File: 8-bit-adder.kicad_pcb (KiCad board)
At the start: 2 copper layers, 109.2 x 88.9 mm, 211 parts, among them J1 J2-2_pole_connector, J2 J8-8_bit_bus_connector, J3 J8-8_bit_bus_connector, J4 J8-8_bit_bus_connector, J5 J1-1_bit_bus, Q1 2N7000, Q10 2N7000, Q100 2N7000, Q101 2N7000, Q102 2N7000, Q103 2N7000, Q104 2N7000, Q105 2N7000, Q106 2N7000, Q107 2N7000, Q108 2N7000, Q109 2N7000, Q11 2N7000, Q110 2N7000, Q111 2N7000, Q112 2N7000, Q113 2N7000, Q114 2N7000, Q115 2N7000, Q116 2N7000, Q117 2N7000, Q118 2N7000, Q119 2N7000, Q12 2N7000, Q13 2N7000, Q14 2N7000, Q15 2N7000, Q16 2N7000, Q17 2N7000, Q18 2N7000, Q19 2N7000, Q2 2N7000, Q20 2N7000, Q21 2N7000, Q22 2N7000, Q23 2N7000, Q24 2N7000, Q25 2N7000, Q26 2N7000, Q27 2N7000, Q28 2N7000, Q29 2N7000, Q3 2N7000, Q30 2N7000, Q31 2N7000, Q32 2N7000, Q33 2N7000, Q34 2N7000, Q35 2N7000, Q36 2N7000, Q37 2N7000, Q38 2N7000, Q39 2N7000, Q4 2N7000, Q40 2N7000, Q41 2N7000, Q42 2N7000, Q43 2N7000, Q44 2N7000, Q45 2N7000, Q46 2N7000, Q47 2N7000, Q48 2N7000, Q49 2N7000, Q5 2N7000, Q50 2N7000, Q51 2N7000, Q52 2N7000, Q53 2N7000, Q54 2N7000, Q55 2N7000, Q56 2N7000, Q57 2N7000, Q58 2N7000, Q59 2N7000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

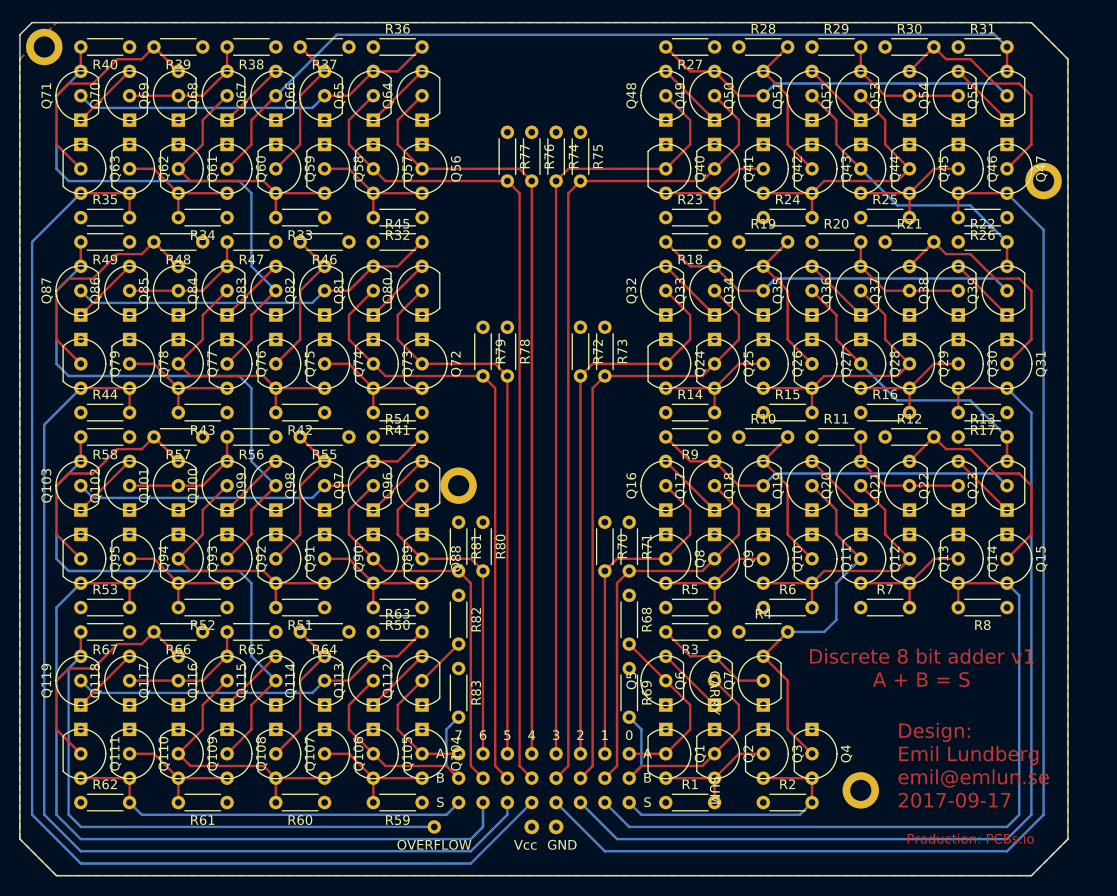
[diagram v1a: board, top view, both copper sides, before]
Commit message: Add carry input to 8 bit adder
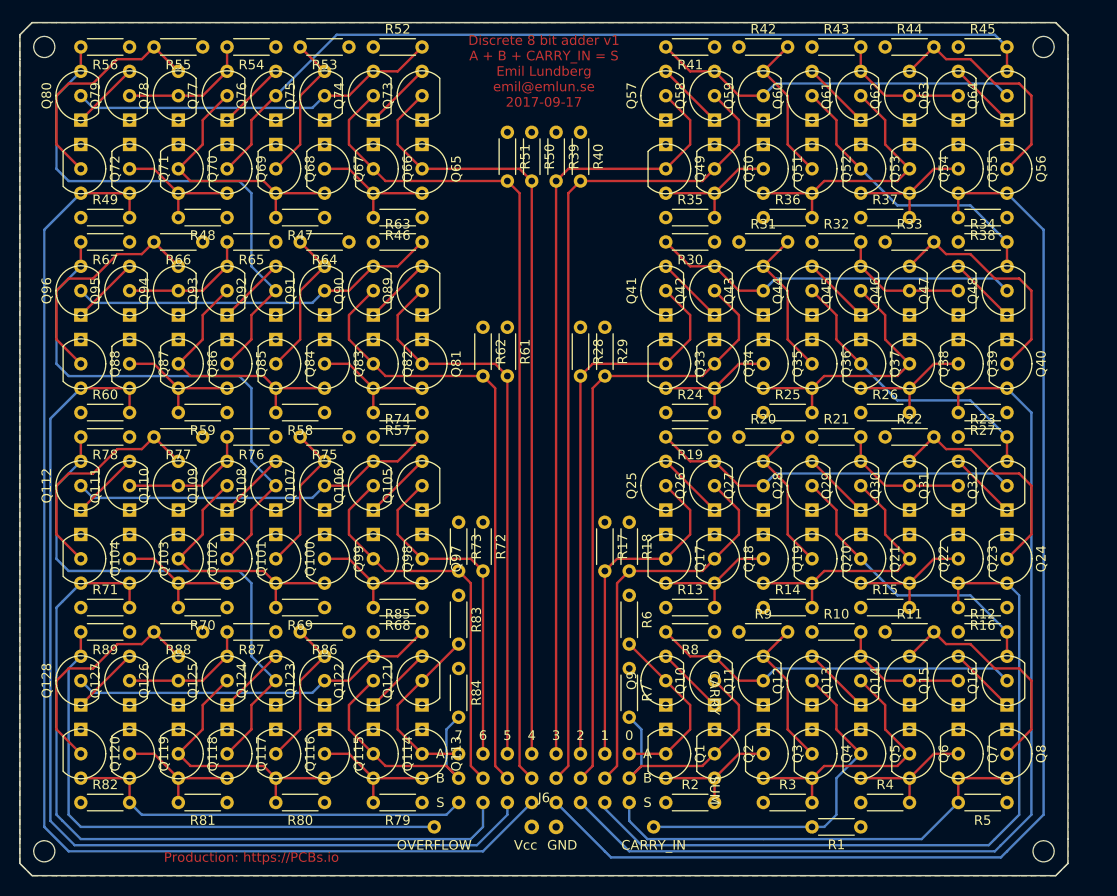
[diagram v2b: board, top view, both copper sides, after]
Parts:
- removed the REF** at (210.8, 77.5)
- removed the REF** at (106.7, 63.5)
- removed the REF** at (149.9, 109.2)
- removed the REF** at (191.8, 141.0)
- added J6: J8-8_bit_bus_connector, emlun:J8-8_bit_bus_connector, F.Cu at (158.8, 142.2)
- added Q120: 2N7000, electrokit:TO-92_Molded_Wide_Inline, F.Cu at (110.5, 135.9)
- added Q121: 2N7000, electrokit:TO-92_Molded_Wide_Inline, F.Cu at (146.1, 130.8)
- added Q122: 2N7000, electrokit:TO-92_Molded_Wide_Inline, F.Cu at (141.0, 130.8)
- added Q123: 2N7000, electrokit:TO-92_Molded_Wide_Inline, F.Cu at (135.9, 130.8)
- added Q124: 2N7000, electrokit:TO-92_Molded_Wide_Inline, F.Cu at (130.8, 130.8)
- added Q125: 2N7000, electrokit:TO-92_Molded_Wide_Inline, F.Cu at (125.7, 130.8)
- added Q126: 2N7000, electrokit:TO-92_Molded_Wide_Inline, F.Cu at (120.7, 130.8)
- added Q127: 2N7000, electrokit:TO-92_Molded_Wide_Inline, F.Cu at (115.6, 130.8)
- added Q128: 2N7000, electrokit:TO-92_Molded_Wide_Inline, F.Cu at (110.5, 130.8)
- added R84: 1M, Resistors_THT:R_Axial_DIN0204_L3.6mm_D1.6mm_P5.08mm_Horizontal, F.Cu at (149.9, 128.3)
- added R85: 1M, Resistors_THT:R_Axial_DIN0204_L3.6mm_D1.6mm_P5.08mm_Horizontal, F.Cu at (141.0, 124.5)
- added R86: 1M, Resistors_THT:R_Axial_DIN0204_L3.6mm_D1.6mm_P5.08mm_Horizontal, F.Cu at (138.4, 124.5)
- added R87: 1M, Resistors_THT:R_Axial_DIN0204_L3.6mm_D1.6mm_P5.08mm_Horizontal, F.Cu at (130.8, 124.5)
- added R88: 1M, Resistors_THT:R_Axial_DIN0204_L3.6mm_D1.6mm_P5.08mm_Horizontal, F.Cu at (123.2, 124.5)
- added R89: 1M, Resistors_THT:R_Axial_DIN0204_L3.6mm_D1.6mm_P5.08mm_Horizontal, F.Cu at (115.6, 124.5)
- added REF**: MountingHole_2.2mm_M2_ISO14580, Mounting_Holes:MountingHole_2.2mm_M2_ISO14580, F.Cu at (210.8, 147.3)
- added REF**: MountingHole_2.2mm_M2, Mounting_Holes:MountingHole_2.2mm_M2, F.Cu at (210.8, 63.5)
- added REF**: MountingHole_2.2mm_M2, Mounting_Holes:MountingHole_2.2mm_M2, F.Cu at (106.7, 63.5)
- added REF**: MountingHole_2.2mm_M2, Mounting_Holes:MountingHole_2.2mm_M2, F.Cu at (106.7, 147.3)
- J2: value J8-8_bit_bus_connector -> J1-1_bit_bus; footprint emlun:J8-8_bit_bus_connector -> emlun:J1-1_bit_bus
- moved R44 92.1 mm to (194.3, 63.5)
- moved Q63 91.6 mm to (201.9, 69.8), turned to 90 degrees
- moved Q62 81.4 mm to (196.8, 69.8), turned to 90 degrees
- moved R38 78.2 mm to (207.0, 81.3)
- moved R34 76.2 mm to (201.9, 83.8), turned to 0 degrees
- moved R43 71.9 mm to (186.7, 63.5), turned to 0 degrees
- moved Q61 71.3 mm to (191.8, 69.8), turned to 90 degrees
- moved R62 64.9 mm to (152.4, 92.7), turned to 270 degrees
- moved R53 64.8 mm to (138.4, 63.5), turned to 180 degrees
- moved R45 64.3 mm to (201.9, 63.5)
- moved Q60 61.2 mm to (186.7, 69.8), turned to 90 degrees
- moved R35 61.0 mm to (171.4, 81.3)
- moved Q56 61.0 mm to (207.0, 74.9)
- moved Q64 61.0 mm to (207.0, 69.8)
- moved R52 60.4 mm to (141.0, 63.5), turned to 0 degrees
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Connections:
- J2 pad 1: /a1 -> /c
- J3 pad 0: /S0 -> /a0
- J3 pad 1: /S1 -> /a1
- J3 pad 2: /S2 -> /a2
- J3 pad 3: /S3 -> /a3
- J3 pad 4: /S4 -> /a4
- J3 pad 5: /S5 -> /a5
- J3 pad 6: /S6 -> /a6
- J3 pad 7: /S7 -> /a7
- J4 pad 0: /b0 -> /S0
- J4 pad 1: /b1 -> /S1
- J4 pad 2: /b2 -> /S2
- J4 pad 3: /b3 -> /S3
- J4 pad 4: /b4 -> /S4
- J4 pad 5: /b5 -> /S5
- J4 pad 6: /b6 -> /S6
- J4 pad 7: /b7 -> /S7
- Q10 pad 1: GND -> Net-(Q10-Pad1)
- Q10 pad 2: Net-(Q10-Pad2) -> /b0
- Q100 pad 1: Net-(Q100-Pad1) -> GND
- Q101 pad 2: Net-(Q100-Pad3) -> /C5
- Q102 pad 3: Net-(Q102-Pad3) -> Net-(Q101-Pad3)
- Q103 pad 1: Net-(Q102-Pad3) -> GND
- Q103 pad 2: Net-(Q103-Pad2) -> Net-(Q101-Pad3)
- Q103 pad 3: /C6 -> /S6
- Q104 pad 2: /a7 -> Net-(Q104-Pad2)
- Q104 pad 3: Net-(Q104-Pad3) -> /S6
- Q105 pad 2: /b7 -> /a6
- Q105 pad 3: Net-(Q104-Pad3) -> Net-(Q105-Pad3)
- Q106 pad 1: GND -> Net-(Q105-Pad3)
- Q106 pad 2: Net-(Q104-Pad3) -> /b6
- Q107 pad 2: Net-(Q107-Pad2) -> Net-(Q106-Pad3)
- Q107 pad 3: Net-(Q106-Pad3) -> Net-(Q100-Pad2)
- Q108 pad 2: /C6 -> /C5
- Q109 pad 1: GND -> Net-(Q108-Pad3)
- Q109 pad 2: Net-(Q106-Pad3) -> Net-(Q100-Pad3)
- Q109 pad 3: Net-(Q108-Pad3) -> Net-(Q109-Pad3)
- Q11 pad 2: Net-(Q11-Pad2) -> Net-(Q10-Pad3)
- Q11 pad 3: Net-(Q10-Pad3) -> Net-(Q11-Pad3)
- Q110 pad 2: Net-(Q108-Pad3) -> Net-(Q109-Pad3)
- Q110 pad 3: /S7 -> Net-(Q104-Pad2)
- Q111 pad 2: Net-(Q111-Pad2) -> Net-(Q109-Pad3)
- Q111 pad 3: /S7 -> Net-(Q111-Pad3)
- Q112 pad 1: GND -> Net-(Q111-Pad3)
- Q112 pad 2: /a7 -> Net-(Q106-Pad3)
- Q112 pad 3: Net-(Q112-Pad3) -> /C6
- Q113 pad 1: Net-(Q112-Pad3) -> GND
- Q113 pad 2: /b7 -> /a7
- Q114 pad 2: Net-(Q113-Pad3) -> /b7
- Q114 pad 3: Net-(Q107-Pad2) -> Net-(Q113-Pad3)
- Q115 pad 2: /C6 -> Net-(Q113-Pad3)
- Q116 pad 1: Net-(Q115-Pad3) -> GND
- Q116 pad 2: Net-(Q106-Pad3) -> Net-(Q116-Pad2)
- Q116 pad 3: Net-(Q116-Pad3) -> Net-(Q115-Pad3)
- Q117 pad 2: Net-(Q116-Pad3) -> /C6
- Q117 pad 3: Net-(Q111-Pad2) -> Net-(Q117-Pad3)
- Q118 pad 2: Net-(Q116-Pad3) -> Net-(Q115-Pad3)
- Q118 pad 3: Net-(Q118-Pad3) -> Net-(Q117-Pad3)
- Q119 pad 1: Net-(Q118-Pad3) -> GND
- Q119 pad 2: Net-(Q113-Pad3) -> Net-(Q117-Pad3)
- Q119 pad 3: /C7 -> /S7
- Q12 pad 2: /C0 -> /c
- Q13 pad 1: GND -> Net-(Q12-Pad3)
- Q13 pad 2: Net-(Q10-Pad3) -> Net-(Q13-Pad2)
- Q13 pad 3: Net-(Q12-Pad3) -> Net-(Q13-Pad3)
- Q14 pad 2: Net-(Q12-Pad3) -> Net-(Q13-Pad3)
- Q14 pad 3: /S1 -> Net-(Q14-Pad3)
- Q15 pad 2: Net-(Q15-Pad2) -> Net-(Q13-Pad3)
- Q15 pad 3: /S1 -> Net-(Q15-Pad3)
- Q16 pad 1: GND -> Net-(Q15-Pad3)
- Q16 pad 2: /a1 -> Net-(Q10-Pad3)
- Q16 pad 3: Net-(Q16-Pad3) -> /C0
- Q17 pad 1: Net-(Q16-Pad3) -> GND
- Q17 pad 2: /b1 -> /a1
- Q18 pad 2: Net-(Q17-Pad3) -> /b1
- Q18 pad 3: Net-(Q11-Pad2) -> Net-(Q17-Pad3)
- Q19 pad 2: /C0 -> Net-(Q17-Pad3)
- Q20 pad 1: Net-(Q19-Pad3) -> GND
- Q20 pad 2: Net-(Q10-Pad3) -> Net-(Q20-Pad2)
- Q20 pad 3: Net-(Q20-Pad3) -> Net-(Q19-Pad3)
- Q21 pad 2: Net-(Q20-Pad3) -> /C0
- Q21 pad 3: Net-(Q15-Pad2) -> Net-(Q21-Pad3)
- Q22 pad 2: Net-(Q20-Pad3) -> Net-(Q19-Pad3)
- Q22 pad 3: Net-(Q22-Pad3) -> Net-(Q21-Pad3)
- Q23 pad 1: Net-(Q22-Pad3) -> GND
- Q23 pad 2: Net-(Q17-Pad3) -> Net-(Q21-Pad3)
- Q23 pad 3: /C1 -> /S1
- Q24 pad 2: /a2 -> Net-(Q24-Pad2)
- Q24 pad 3: Net-(Q24-Pad3) -> /S1
- Q25 pad 2: /b2 -> /a1
- Q25 pad 3: Net-(Q24-Pad3) -> Net-(Q25-Pad3)
- Q26 pad 1: GND -> Net-(Q25-Pad3)
- Q26 pad 2: Net-(Q24-Pad3) -> /b1
- Q27 pad 2: Net-(Q27-Pad2) -> Net-(Q26-Pad3)
- Q27 pad 3: Net-(Q26-Pad3) -> Net-(Q20-Pad2)
- Q28 pad 2: /C1 -> /C0
- Q29 pad 1: GND -> Net-(Q28-Pad3)
- Q29 pad 2: Net-(Q26-Pad3) -> Net-(Q19-Pad3)
- Q29 pad 3: Net-(Q28-Pad3) -> Net-(Q29-Pad3)
- Q3 pad 3: /S0 -> Net-(Q13-Pad2)
- Q30 pad 2: Net-(Q28-Pad3) -> Net-(Q29-Pad3)
- Q30 pad 3: /S2 -> Net-(Q24-Pad2)
- Q31 pad 2: Net-(Q31-Pad2) -> Net-(Q29-Pad3)
- Q31 pad 3: /S2 -> Net-(Q31-Pad3)
- Q32 pad 1: GND -> Net-(Q31-Pad3)
- Q32 pad 2: /a2 -> Net-(Q26-Pad3)
- Q32 pad 3: Net-(Q32-Pad3) -> /C1
- Q33 pad 1: Net-(Q32-Pad3) -> GND
- Q33 pad 2: /b2 -> /a2
- Q34 pad 2: Net-(Q33-Pad3) -> /b2
- Q34 pad 3: Net-(Q27-Pad2) -> Net-(Q33-Pad3)
- Q35 pad 2: /C1 -> Net-(Q33-Pad3)
- Q36 pad 1: Net-(Q35-Pad3) -> GND
- Q36 pad 2: Net-(Q26-Pad3) -> Net-(Q36-Pad2)
- Q36 pad 3: Net-(Q36-Pad3) -> Net-(Q35-Pad3)
- Q37 pad 2: Net-(Q36-Pad3) -> /C1
- Q37 pad 3: Net-(Q31-Pad2) -> Net-(Q37-Pad3)
- Q38 pad 2: Net-(Q36-Pad3) -> Net-(Q35-Pad3)
- Q38 pad 3: Net-(Q38-Pad3) -> Net-(Q37-Pad3)
- Q39 pad 1: Net-(Q38-Pad3) -> GND
- Q39 pad 2: Net-(Q33-Pad3) -> Net-(Q37-Pad3)
- Q39 pad 3: /C2 -> /S2
- Q4 pad 2: /C0 -> Net-(Q11-Pad3)
- Q4 pad 3: /S0 -> Net-(Q13-Pad2)
- Q40 pad 2: /a3 -> Net-(Q40-Pad2)
- Q40 pad 3: Net-(Q40-Pad3) -> /S2
- Q41 pad 2: /b3 -> /a2
- Q41 pad 3: Net-(Q40-Pad3) -> Net-(Q41-Pad3)
- Q42 pad 1: GND -> Net-(Q41-Pad3)
- Q42 pad 2: Net-(Q40-Pad3) -> /b2
- Q43 pad 2: Net-(Q43-Pad2) -> Net-(Q42-Pad3)
- Q43 pad 3: Net-(Q42-Pad3) -> Net-(Q36-Pad2)
- Q44 pad 2: /C2 -> /C1
- Q45 pad 1: GND -> Net-(Q44-Pad3)
- Q45 pad 2: Net-(Q42-Pad3) -> Net-(Q35-Pad3)
- Q45 pad 3: Net-(Q44-Pad3) -> Net-(Q45-Pad3)
- Q46 pad 2: Net-(Q44-Pad3) -> Net-(Q45-Pad3)
- Q46 pad 3: /S3 -> Net-(Q40-Pad2)
- Q47 pad 2: Net-(Q47-Pad2) -> Net-(Q45-Pad3)
- Q47 pad 3: /S3 -> Net-(Q47-Pad3)
- Q48 pad 1: GND -> Net-(Q47-Pad3)
- Q48 pad 2: /a3 -> Net-(Q42-Pad3)
- Q48 pad 3: Net-(Q48-Pad3) -> /C2
- Q49 pad 1: Net-(Q48-Pad3) -> GND
- Q49 pad 2: /b3 -> /a3
- Q5 pad 2: /a0 -> /c
- Q50 pad 2: Net-(Q49-Pad3) -> /b3
- Q50 pad 3: Net-(Q43-Pad2) -> Net-(Q49-Pad3)
- Q51 pad 2: /C2 -> Net-(Q49-Pad3)
- Q52 pad 1: Net-(Q51-Pad3) -> GND
- Q52 pad 2: Net-(Q42-Pad3) -> Net-(Q52-Pad2)
- Q52 pad 3: Net-(Q52-Pad3) -> Net-(Q51-Pad3)
- Q53 pad 2: Net-(Q52-Pad3) -> /C2
- Q53 pad 3: Net-(Q47-Pad2) -> Net-(Q53-Pad3)
- Q54 pad 2: Net-(Q52-Pad3) -> Net-(Q51-Pad3)
- Q54 pad 3: Net-(Q54-Pad3) -> Net-(Q53-Pad3)
- Q55 pad 1: Net-(Q54-Pad3) -> GND
- Q55 pad 2: Net-(Q49-Pad3) -> Net-(Q53-Pad3)
- Q55 pad 3: /C3 -> /S3
- Q56 pad 2: /a4 -> Net-(Q56-Pad2)
- Q56 pad 3: Net-(Q56-Pad3) -> /S3
- Q57 pad 2: /b4 -> /a3
- Q57 pad 3: Net-(Q56-Pad3) -> Net-(Q57-Pad3)
- Q58 pad 1: GND -> Net-(Q57-Pad3)
- Q58 pad 2: Net-(Q56-Pad3) -> /b3
- Q59 pad 2: Net-(Q59-Pad2) -> Net-(Q58-Pad3)
- Q59 pad 3: Net-(Q58-Pad3) -> Net-(Q52-Pad2)
- Q6 pad 1: Net-(Q5-Pad3) -> GND
- Q6 pad 2: /b0 -> Net-(Q13-Pad2)
- Q6 pad 3: Net-(Q6-Pad3) -> Net-(Q5-Pad3)
- Q60 pad 2: /C3 -> /C2
- Q61 pad 1: GND -> Net-(Q60-Pad3)
- Q61 pad 2: Net-(Q58-Pad3) -> Net-(Q51-Pad3)
- Q61 pad 3: Net-(Q60-Pad3) -> Net-(Q61-Pad3)
- Q62 pad 2: Net-(Q60-Pad3) -> Net-(Q61-Pad3)
- Q62 pad 3: /S4 -> Net-(Q56-Pad2)
- Q63 pad 2: Net-(Q63-Pad2) -> Net-(Q61-Pad3)
- Q63 pad 3: /S4 -> Net-(Q63-Pad3)
- Q64 pad 1: GND -> Net-(Q63-Pad3)
- Q64 pad 2: /a4 -> Net-(Q58-Pad3)
- Q64 pad 3: Net-(Q64-Pad3) -> /C3
- Q65 pad 1: Net-(Q64-Pad3) -> GND
- Q65 pad 2: /b4 -> /a4
- Q66 pad 2: Net-(Q65-Pad3) -> /b4
- Q66 pad 3: Net-(Q59-Pad2) -> Net-(Q65-Pad3)
- Q67 pad 2: /C3 -> Net-(Q65-Pad3)
- Q68 pad 1: Net-(Q67-Pad3) -> GND
- Q68 pad 2: Net-(Q58-Pad3) -> Net-(Q68-Pad2)
- Q68 pad 3: Net-(Q68-Pad3) -> Net-(Q67-Pad3)
- Q69 pad 2: Net-(Q68-Pad3) -> /C3
- Q69 pad 3: Net-(Q63-Pad2) -> Net-(Q69-Pad3)
- Q7 pad 2: Net-(Q6-Pad3) -> Net-(Q5-Pad3)
- Q7 pad 3: /C0 -> /S0
- Q70 pad 2: Net-(Q68-Pad3) -> Net-(Q67-Pad3)
- Q70 pad 3: Net-(Q70-Pad3) -> Net-(Q69-Pad3)
- Q71 pad 1: Net-(Q70-Pad3) -> GND
- Q71 pad 2: Net-(Q65-Pad3) -> Net-(Q69-Pad3)
- Q71 pad 3: /C4 -> /S4
- Q72 pad 2: /a5 -> Net-(Q72-Pad2)
- Q72 pad 3: Net-(Q72-Pad3) -> /S4
- Q73 pad 2: /b5 -> /a4
- Q73 pad 3: Net-(Q72-Pad3) -> Net-(Q73-Pad3)
- Q74 pad 1: GND -> Net-(Q73-Pad3)
- Q74 pad 2: Net-(Q72-Pad3) -> /b4
- Q75 pad 2: Net-(Q75-Pad2) -> Net-(Q74-Pad3)
- Q75 pad 3: Net-(Q74-Pad3) -> Net-(Q68-Pad2)
- Q76 pad 2: /C4 -> /C3
- Q77 pad 1: GND -> Net-(Q76-Pad3)
- Q77 pad 2: Net-(Q74-Pad3) -> Net-(Q67-Pad3)
- Q77 pad 3: Net-(Q76-Pad3) -> Net-(Q77-Pad3)
- Q78 pad 2: Net-(Q76-Pad3) -> Net-(Q77-Pad3)
- Q78 pad 3: /S5 -> Net-(Q72-Pad2)
- Q79 pad 2: Net-(Q79-Pad2) -> Net-(Q77-Pad3)
- Q79 pad 3: /S5 -> Net-(Q79-Pad3)
- Q8 pad 2: /a1 -> Net-(Q14-Pad3)
- Q8 pad 3: Net-(Q10-Pad2) -> /S0
- Q80 pad 1: GND -> Net-(Q79-Pad3)
- Q80 pad 2: /a5 -> Net-(Q74-Pad3)
- Q80 pad 3: Net-(Q80-Pad3) -> /C4
- Q81 pad 1: Net-(Q80-Pad3) -> GND
- Q81 pad 2: /b5 -> /a5
- Q82 pad 2: Net-(Q81-Pad3) -> /b5
- Q82 pad 3: Net-(Q75-Pad2) -> Net-(Q81-Pad3)
- Q83 pad 2: /C4 -> Net-(Q81-Pad3)
- Q84 pad 1: Net-(Q83-Pad3) -> GND
- Q84 pad 2: Net-(Q74-Pad3) -> Net-(Q84-Pad2)
- Q84 pad 3: Net-(Q84-Pad3) -> Net-(Q83-Pad3)
- Q85 pad 2: Net-(Q84-Pad3) -> /C4
- Q85 pad 3: Net-(Q79-Pad2) -> Net-(Q85-Pad3)
- Q86 pad 2: Net-(Q84-Pad3) -> Net-(Q83-Pad3)
- Q86 pad 3: Net-(Q86-Pad3) -> Net-(Q85-Pad3)
- Q87 pad 1: Net-(Q86-Pad3) -> GND
- Q87 pad 2: Net-(Q81-Pad3) -> Net-(Q85-Pad3)
- Q87 pad 3: /C5 -> /S5
- Q88 pad 2: /a6 -> Net-(Q88-Pad2)
- Q88 pad 3: Net-(Q88-Pad3) -> /S5
- Q89 pad 2: /b6 -> /a5
- Q89 pad 3: Net-(Q88-Pad3) -> Net-(Q89-Pad3)
- Q9 pad 2: /b1 -> /a0
- Q9 pad 3: Net-(Q10-Pad2) -> Net-(Q10-Pad1)
- Q90 pad 1: GND -> Net-(Q89-Pad3)
- Q90 pad 2: Net-(Q88-Pad3) -> /b5
- Q90 pad 3: Net-(Q100-Pad2) -> Net-(Q90-Pad3)
- Q91 pad 2: Net-(Q91-Pad2) -> Net-(Q90-Pad3)
- Q91 pad 3: Net-(Q100-Pad2) -> Net-(Q84-Pad2)
- Q92 pad 2: /C5 -> /C4
- Q93 pad 1: GND -> Net-(Q92-Pad3)
- Q93 pad 2: Net-(Q100-Pad2) -> Net-(Q83-Pad3)
- Q93 pad 3: Net-(Q92-Pad3) -> Net-(Q93-Pad3)
- Q94 pad 2: Net-(Q92-Pad3) -> Net-(Q93-Pad3)
- Q94 pad 3: /S6 -> Net-(Q88-Pad2)
- Q95 pad 2: Net-(Q101-Pad3) -> Net-(Q93-Pad3)
- Q95 pad 3: /S6 -> Net-(Q95-Pad3)
- Q96 pad 1: GND -> Net-(Q95-Pad3)
- Q96 pad 2: /a6 -> Net-(Q90-Pad3)
- Q96 pad 3: Net-(Q96-Pad3) -> /C5
- Q97 pad 1: Net-(Q96-Pad3) -> GND
- Q97 pad 2: /b6 -> /a6
- Q97 pad 3: Net-(Q103-Pad2) -> Net-(Q97-Pad3)
- Q98 pad 2: Net-(Q103-Pad2) -> /b6
- Q98 pad 3: Net-(Q91-Pad2) -> Net-(Q97-Pad3)
- Q99 pad 2: /C5 -> Net-(Q97-Pad3)
- Q99 pad 3: Net-(Q100-Pad1) -> Net-(Q100-Pad3)
- R1 pad 1: VCC -> GND
- R1 pad 2: Net-(Q1-Pad3) -> /c
- R10 pad 2: Net-(Q11-Pad2) -> Net-(Q13-Pad3)
- R11 pad 2: Net-(Q20-Pad3) -> Net-(Q14-Pad3)
- R12 pad 2: Net-(Q15-Pad2) -> /C0
- R13 pad 2: /C1 -> Net-(Q17-Pad3)
- R14 pad 2: Net-(Q24-Pad3) -> Net-(Q19-Pad3)
- R15 pad 2: Net-(Q26-Pad3) -> Net-(Q21-Pad3)
- R16 pad 2: Net-(Q28-Pad3) -> /S1
- R17 pad 1: VCC -> GND
- R17 pad 2: /S2 -> /a1
- R18 pad 1: VCC -> GND
- R18 pad 2: Net-(Q33-Pad3) -> /b1
- R19 pad 2: Net-(Q27-Pad2) -> Net-(Q26-Pad3)
- R2 pad 2: /S0 -> Net-(Q1-Pad3)
- R20 pad 2: Net-(Q36-Pad3) -> Net-(Q20-Pad2)
- R21 pad 2: Net-(Q31-Pad2) -> Net-(Q29-Pad3)
- R22 pad 2: /C2 -> Net-(Q24-Pad2)
- R23 pad 2: Net-(Q40-Pad3) -> /C1
- R24 pad 2: Net-(Q42-Pad3) -> Net-(Q33-Pad3)
- R25 pad 2: Net-(Q44-Pad3) -> Net-(Q35-Pad3)
- R26 pad 2: /S3 -> Net-(Q37-Pad3)
- R27 pad 2: Net-(Q49-Pad3) -> /S2
- R28 pad 1: VCC -> GND
- R28 pad 2: Net-(Q43-Pad2) -> /a2
- R29 pad 1: VCC -> GND
- R29 pad 2: Net-(Q52-Pad3) -> /b2
- R3 pad 2: Net-(Q6-Pad3) -> Net-(Q13-Pad2)
- R30 pad 2: Net-(Q47-Pad2) -> Net-(Q42-Pad3)
- R31 pad 2: /C3 -> Net-(Q36-Pad2)
- R32 pad 2: Net-(Q56-Pad3) -> Net-(Q45-Pad3)
- R33 pad 2: Net-(Q58-Pad3) -> Net-(Q40-Pad2)
- R34 pad 2: Net-(Q60-Pad3) -> /C2
- R35 pad 2: /S4 -> Net-(Q49-Pad3)
- R36 pad 2: Net-(Q65-Pad3) -> Net-(Q51-Pad3)
- R37 pad 2: Net-(Q59-Pad2) -> Net-(Q53-Pad3)
- R38 pad 2: Net-(Q68-Pad3) -> /S3
- R39 pad 1: VCC -> GND
- R39 pad 2: Net-(Q63-Pad2) -> /a3
- R4 pad 2: /C0 -> Net-(Q5-Pad3)
- R40 pad 1: VCC -> GND
- R40 pad 2: /C4 -> /b3
- R41 pad 2: Net-(Q72-Pad3) -> Net-(Q58-Pad3)
- R42 pad 2: Net-(Q74-Pad3) -> Net-(Q52-Pad2)
- R43 pad 2: Net-(Q76-Pad3) -> Net-(Q61-Pad3)
- R44 pad 2: /S5 -> Net-(Q56-Pad2)
- R45 pad 2: Net-(Q81-Pad3) -> /C3
- R46 pad 2: Net-(Q75-Pad2) -> Net-(Q65-Pad3)
- R47 pad 2: Net-(Q84-Pad3) -> Net-(Q67-Pad3)
- R48 pad 2: Net-(Q79-Pad2) -> Net-(Q69-Pad3)
- R49 pad 2: /C5 -> /S4
- R5 pad 2: Net-(Q10-Pad2) -> /S0
- R50 pad 1: VCC -> GND
- R50 pad 2: Net-(Q88-Pad3) -> /a4
- R51 pad 1: VCC -> GND
- R51 pad 2: Net-(Q100-Pad2) -> /b4
- R52 pad 2: Net-(Q92-Pad3) -> Net-(Q74-Pad3)
- R53 pad 2: /S6 -> Net-(Q68-Pad2)
- R54 pad 2: Net-(Q103-Pad2) -> Net-(Q77-Pad3)
- R55 pad 2: Net-(Q91-Pad2) -> Net-(Q72-Pad2)
- R56 pad 2: Net-(Q100-Pad3) -> /C4
- R57 pad 2: Net-(Q101-Pad3) -> Net-(Q81-Pad3)
- R58 pad 2: /C6 -> Net-(Q83-Pad3)
- R59 pad 2: Net-(Q104-Pad3) -> Net-(Q85-Pad3)
- R6 pad 1: VCC -> GND
- R6 pad 2: Net-(Q10-Pad3) -> /a0
- R60 pad 2: Net-(Q106-Pad3) -> /S5
- R61 pad 1: VCC -> GND
- R61 pad 2: Net-(Q108-Pad3) -> /a5
- R62 pad 1: VCC -> GND
- R62 pad 2: /S7 -> /b5
- R63 pad 2: Net-(Q113-Pad3) -> Net-(Q90-Pad3)
- R64 pad 2: Net-(Q107-Pad2) -> Net-(Q84-Pad2)
- R65 pad 2: Net-(Q116-Pad3) -> Net-(Q93-Pad3)
- R66 pad 2: Net-(Q111-Pad2) -> Net-(Q88-Pad2)
- R67 pad 2: /C7 -> /C5
- R68 pad 1: GND -> VCC
- R68 pad 2: /a0 -> Net-(Q97-Pad3)
- R69 pad 1: GND -> VCC
- R69 pad 2: /b0 -> Net-(Q100-Pad3)
- R7 pad 1: VCC -> GND
- R7 pad 2: Net-(Q12-Pad3) -> /b0
- R70 pad 1: GND -> VCC
- R70 pad 2: /a1 -> Net-(Q101-Pad3)
- R71 pad 1: GND -> VCC
- R71 pad 2: /b1 -> /S6
- R72 pad 2: /a2 -> /a6
- R73 pad 2: /b2 -> /b6
- R74 pad 1: GND -> VCC
- R74 pad 2: /a3 -> Net-(Q106-Pad3)
- R75 pad 1: GND -> VCC
- R75 pad 2: /b3 -> Net-(Q100-Pad2)
- R76 pad 1: GND -> VCC
- R76 pad 2: /a4 -> Net-(Q109-Pad3)
- R77 pad 1: GND -> VCC
- R77 pad 2: /b4 -> Net-(Q104-Pad2)
- R78 pad 1: GND -> VCC
- R78 pad 2: /a5 -> /C6
- R79 pad 1: GND -> VCC
- R79 pad 2: /b5 -> Net-(Q113-Pad3)
- R8 pad 2: /S1 -> Net-(Q10-Pad3)
- R80 pad 1: GND -> VCC
- R80 pad 2: /a6 -> Net-(Q115-Pad3)
- R81 pad 1: GND -> VCC
- R81 pad 2: /b6 -> Net-(Q117-Pad3)
- R82 pad 1: GND -> VCC
- R82 pad 2: /a7 -> /S7
- R83 pad 2: /b7 -> /a7
- R9 pad 2: Net-(Q17-Pad3) -> Net-(Q11-Pad3)
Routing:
- net Net-(Q122-Pad3): track 0.00 -> 38.7 mm
- net Net-(Q90-Pad3): track 0.00 -> 38.7 mm
- net Net-(Q103-Pad2): track 38.7 -> 0.00 mm
- net /c: track 0.00 -> 36.7 mm
- net Net-(Q13-Pad2): track 0.00 -> 28.6 mm
- net Net-(Q33-Pad3): track 38.7 -> 13.8 mm
- net Net-(Q81-Pad3): track 38.7 -> 13.8 mm
- net Net-(Q113-Pad3): track 38.7 -> 13.8 mm
- net Net-(Q65-Pad3): track 38.7 -> 13.8 mm
- net Net-(Q49-Pad3): track 38.7 -> 13.8 mm
- net Net-(Q17-Pad3): track 38.7 -> 13.8 mm
- net Net-(Q14-Pad3): track 0.00 -> 24.5 mm
- net Net-(Q40-Pad2): track 0.00 -> 24.5 mm
- net Net-(Q56-Pad2): track 0.00 -> 24.5 mm
- net Net-(Q47-Pad2): track 24.5 -> 0.00 mm
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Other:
- outline, holes or cut-outs redrawn
- board text added: "CARRY_IN"
- board text added: "Discrete 8 bit adder v1 A + B + CARRY_IN = S Emil Lundberg emil@emlun.se 2017-09-17"
- board text added: "Production: https://PCBs.io"
- board text removed: "Design: Emil Lundberg emil@emlun.se 2017-09-17"
- board text removed: "Discrete 8 bit adder v1 A + B = S"
- board text removed: "Production: PCBs.io"
